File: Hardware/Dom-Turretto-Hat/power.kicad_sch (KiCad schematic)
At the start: 14 parts

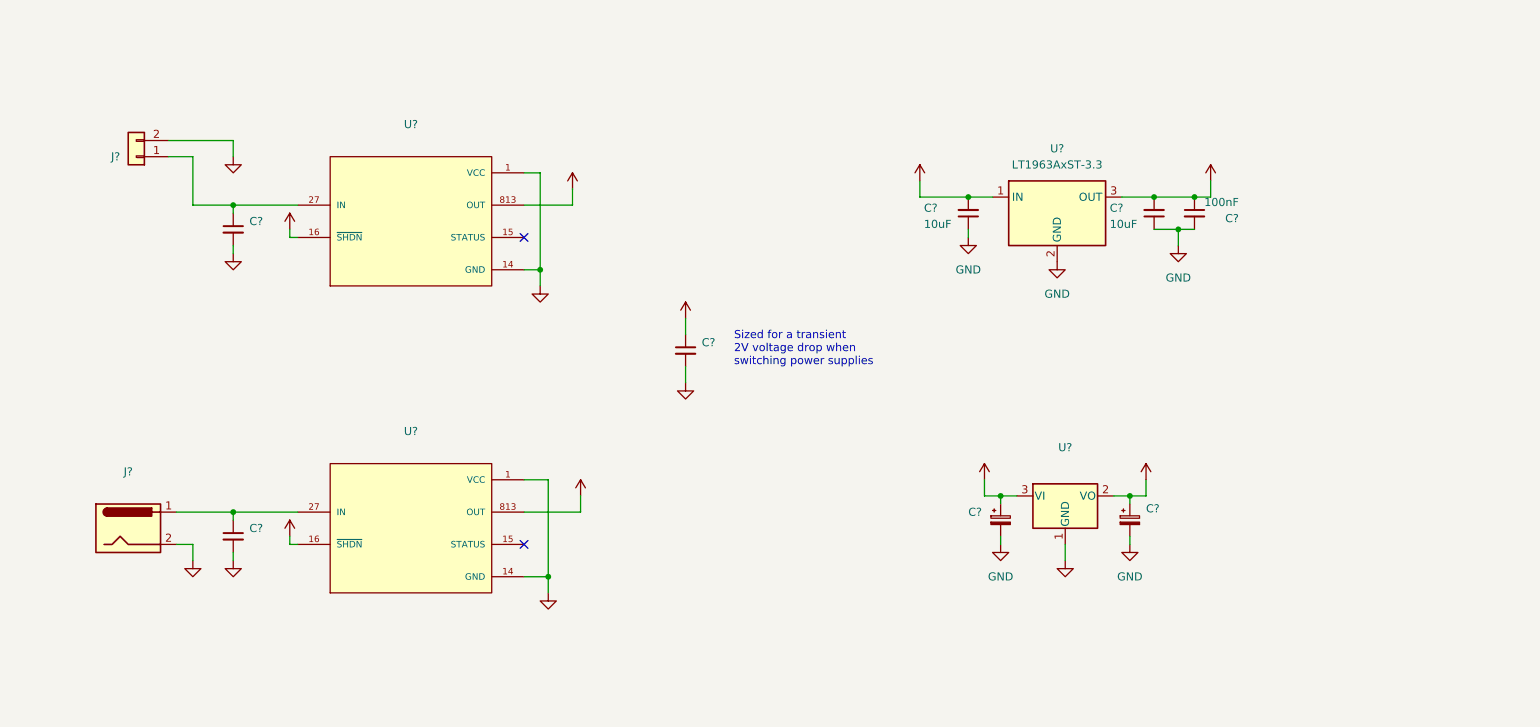
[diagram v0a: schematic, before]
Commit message: Add stepper motor drivers
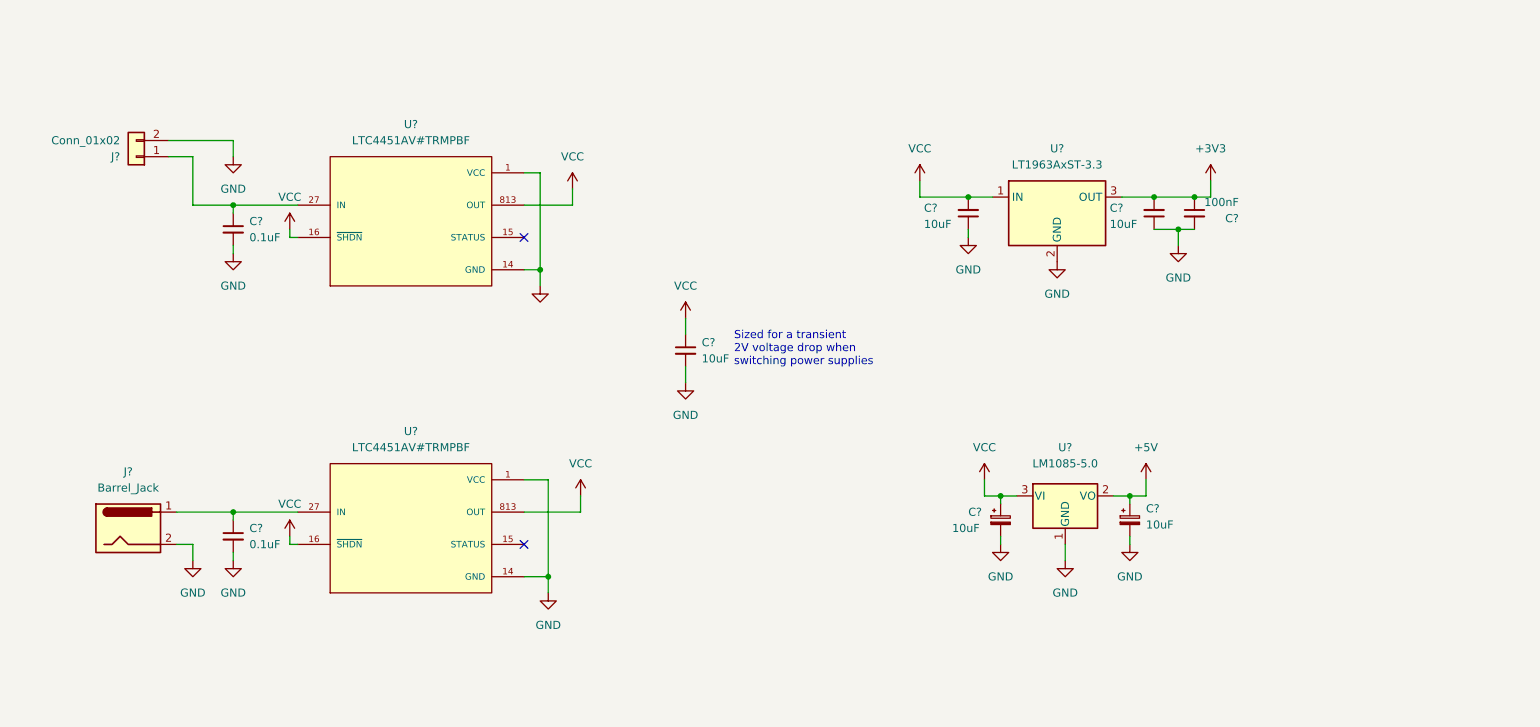
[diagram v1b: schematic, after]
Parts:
- C? (x3): value (none) -> 10uF
- C? (x2): value (none) -> 0.1uF
- J?: value (none) -> Conn_01x02
- J?: value (none) -> Barrel_Jack
- U?: value (none) -> LM1085-5.0
- U? (x2): value (none) -> LTC4451AV#TRMPBF; footprint (none) -> IC_LTC4451AV#TRMPBF
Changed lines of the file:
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@@
       (effects (font (size 1.27 1.27)) hide)
     )
-    (property "Value" "" (id 1) (at 179.07 60.96 0))
+    (property "Value" "VCC" (id 1) (at 179.07 60.96 0))
     (property "Footprint" "" (id 2) (at 179.07 66.04 0)
       (effects (font (size 1.27 1.27)) hide)
@@
       (effects (font (size 1.27 1.27)) (justify left))
     )
-    (property "Value" "" (id 1) (at 184.15 120.65 0)
+    (property "Value" "10uF" (id 1) (at 184.15 120.65 0)
       (effects (font (size 1.27 1.27)) (justify left))
     )
@@
       (effects (font (size 1.27 1.27)) hide)
     )
-    (property "Value" "" (id 1) (at 120.65 135.89 0))
+    (property "Value" "GND" (id 1) (at 120.65 135.89 0))
     (property "Footprint" "" (id 2) (at 120.65 130.81 0)
       (effects (font (size 1.27 1.27)) hide)
@@
       (effects (font (size 1.27 1.27)) hide)
     )
-    (property "Value" "" (id 1) (at 124.46 62.23 0))
+    (property "Value" "VCC" (id 1) (at 124.46 62.23 0))
     (property "Footprint" "" (id 2) (at 124.46 67.31 0)
       (effects (font (size 1.27 1.27)) hide)
@@
     (in_bom yes) (on_board yes) (fields_autoplaced)
     (property "Reference" "U?" (id 0) (at 201.93 107.95 0))
-    (property "Value" "" (id 1) (at 201.93 110.49 0))
+    (property "Value" "LM1085-5.0" (id 1) (at 201.93 110.49 0))
     (property "Footprint" "" (id 2) (at 201.93 109.22 0)
       (effects (font (size 1.27 1.27) italic) hide)
@@
       (effects (font (size 1.27 1.27)) hide)
     )
-    (property "Value" "" (id 1) (at 201.93 130.81 0))
+    (property "Value" "GND" (id 1) (at 201.93 130.81 0))
     (property "Footprint" "" (id 2) (at 201.93 125.73 0)
       (effects (font (size 1.27 1.27)) hide)
@@
       (effects (font (size 1.27 1.27)) hide)
     )
-    (property "Value" "" (id 1) (at 142.24 102.87 0))
+    (property "Value" "GND" (id 1) (at 142.24 102.87 0))
     (property "Footprint" "" (id 2) (at 142.24 97.79 0)
       (effects (font (size 1.27 1.27)) hide)
@@
       (effects (font (size 1.27 1.27)) (justify left))
     )
-    (property "Value" "" (id 1) (at 144.78 93.9862 0)
+    (property "Value" "10uF" (id 1) (at 144.78 93.9862 0)
       (effects (font (size 1.27 1.27)) (justify left))
     )
@@
       (effects (font (size 1.27 1.27)) hide)
     )
-    (property "Value" "" (id 1) (at 80.01 116.84 0))
+    (property "Value" "VCC" (id 1) (at 80.01 116.84 0))
     (property "Footprint" "" (id 2) (at 80.01 121.92 0)
       (effects (font (size 1.27 1.27)) hide)
@@
       (effects (font (size 1.27 1.27)) (justify left))
     )
-    (property "Value" "" (id 1) (at 214.63 120.1038 0)
+    (property "Value" "10uF" (id 1) (at 214.63 120.1038 0)
       (effects (font (size 1.27 1.27)) (justify left))
     )
@@
       (effects (font (size 1.27 1.27)) hide)
     )
-    (property "Value" "" (id 1) (at 64.77 130.81 0))
+    (property "Value" "GND" (id 1) (at 64.77 130.81 0))
     (property "Footprint" "" (id 2) (at 64.77 125.73 0)
       (effects (font (size 1.27 1.27)) hide)
@@
       (effects (font (size 1.27 1.27)) (justify left))
     )
-    (property "Value" "" (id 1) (at 73.66 123.1962 0)
+    (property "Value" "0.1uF" (id 1) (at 73.66 123.1962 0)
       (effects (font (size 1.27 1.27)) (justify left))
     )
@@
       (effects (font (size 1.27 1.27)) hide)
     )
-    (property "Value" "" (id 1) (at 71.12 130.81 0))
+    (property "Value" "GND" (id 1) (at 71.12 130.81 0))
     (property "Footprint" "" (id 2) (at 71.12 125.73 0)
       (effects (font (size 1.27 1.27)) hide)
@@
       (effects (font (size 1.27 1.27)) hide)
     )
-    (property "Value" "" (id 1) (at 189.23 107.95 0))
+    (property "Value" "VCC" (id 1) (at 189.23 107.95 0))
     (property "Footprint" "" (id 2) (at 189.23 113.03 0)
       (effects (font (size 1.27 1.27)) hide)
@@
       (effects (font (size 1.27 1.27)) hide)
     )
-    (property "Value" "" (id 1) (at 125.73 110.49 0))
+    (property "Value" "VCC" (id 1) (at 125.73 110.49 0))
     (property "Footprint" "" (id 2) (at 125.73 115.57 0)
       (effects (font (size 1.27 1.27)) hide)
@@
     (in_bom yes) (on_board yes) (fields_autoplaced)
     (property "Reference" "U?" (id 0) (at 99.06 57.15 0))
-    (property "Value" "" (id 1) (at 99.06 59.69 0))
-    (property "Footprint" "" (id 2) (at 99.06 72.39 0)
+    (property "Value" "LTC4451AV#TRMPBF" (id 1) (at 99.06 59.69 0))
+    (property "Footprint" "IC_LTC4451AV#TRMPBF" (id 2) (at 99.06 72.39 0)
       (effects (font (size 1.27 1.27)) (justify left bottom) hide)
     )
@@
       (effects (font (size 1.27 1.27)) hide)
     )
-    (property "Value" "" (id 1) (at 224.79 60.96 0))
+    (property "Value" "+3V3" (id 1) (at 224.79 60.96 0))
     (property "Footprint" "" (id 2) (at 224.79 66.04 0)
       (effects (font (size 1.27 1.27)) hide)
@@
       (effects (font (size 1.27 1.27)) hide)
     )
-    (property "Value" "" (id 1) (at 80.01 68.58 0))
+    (property "Value" "VCC" (id 1) (at 80.01 68.58 0))
     (property "Footprint" "" (id 2) (at 80.01 73.66 0)
       (effects (font (size 1.27 1.27)) hide)
@@
       (effects (font (size 1.27 1.27)) (justify left))
     )
-    (property "Value" "" (id 1) (at 53.34 59.6901 0)
+    (property "Value" "Conn_01x02" (id 1) (at 53.34 59.6901 0)
       (effects (font (size 1.27 1.27)) (justify left))
     )
@@
       (effects (font (size 1.27 1.27)) hide)
     )
-    (property "Value" "" (id 1) (at 214.63 107.95 0))
+    (property "Value" "+5V" (id 1) (at 214.63 107.95 0))
     (property "Footprint" "" (id 2) (at 214.63 113.03 0)
       (effects (font (size 1.27 1.27)) hide)
@@
       (effects (font (size 1.27 1.27)) hide)
     )
-    (property "Value" "" (id 1) (at 71.12 67.31 0))
+    (property "Value" "GND" (id 1) (at 71.12 67.31 0))
     (property "Footprint" "" (id 2) (at 71.12 62.23 0)
       (effects (font (size 1.27 1.27)) hide)
@@
     (in_bom yes) (on_board yes) (fields_autoplaced)
     (property "Reference" "U?" (id 0) (at 99.06 105.41 0))
-    (property "Value" "" (id 1) (at 99.06 107.95 0))
-    (property "Footprint" "" (id 2) (at 99.06 120.65 0)
+    (property "Value" "LTC4451AV#TRMPBF" (id 1) (at 99.06 107.95 0))
+    (property "Footprint" "IC_LTC4451AV#TRMPBF" (id 2) (at 99.06 120.65 0)
       (effects (font (size 1.27 1.27)) (justify left bottom) hide)
     )
@@
       (effects (font (size 1.27 1.27)) hide)
     )
-    (property "Value" "" (id 1) (at 71.12 82.55 0))
+    (property "Value" "GND" (id 1) (at 71.12 82.55 0))
     (property "Footprint" "" (id 2) (at 71.12 77.47 0)
       (effects (font (size 1.27 1.27)) hide)
@@
       (effects (font (size 1.27 1.27)) hide)
     )
-    (property "Value" "" (id 1) (at 142.24 82.55 0))
+    (property "Value" "VCC" (id 1) (at 142.24 82.55 0))
     (property "Footprint" "" (id 2) (at 142.24 87.63 0)
       (effects (font (size 1.27 1.27)) hide)
@@
     (in_bom yes) (on_board yes) (fields_autoplaced)
     (property "Reference" "J?" (id 0) (at 54.61 111.76 0))
-    (property "Value" "" (id 1) (at 54.61 114.3 0))
+    (property "Value" "Barrel_Jack" (id 1) (at 54.61 114.3 0))
     (property "Footprint" "" (id 2) (at 55.88 121.666 0)
       (effects (font (size 1.27 1.27)) hide)
@@
       (effects (font (size 1.27 1.27)) (justify left))
     )
-    (property "Value" "" (id 1) (at 73.66 74.9362 0)
-      (effects (font (size 1.27 1.27)) (justify left))
-    )
+    (property "Value" "0.1uF" (id 1) (at 73.66 74.9362 0)
+      (effects (font (size 1.27 1.27)) (justify left))
+    )

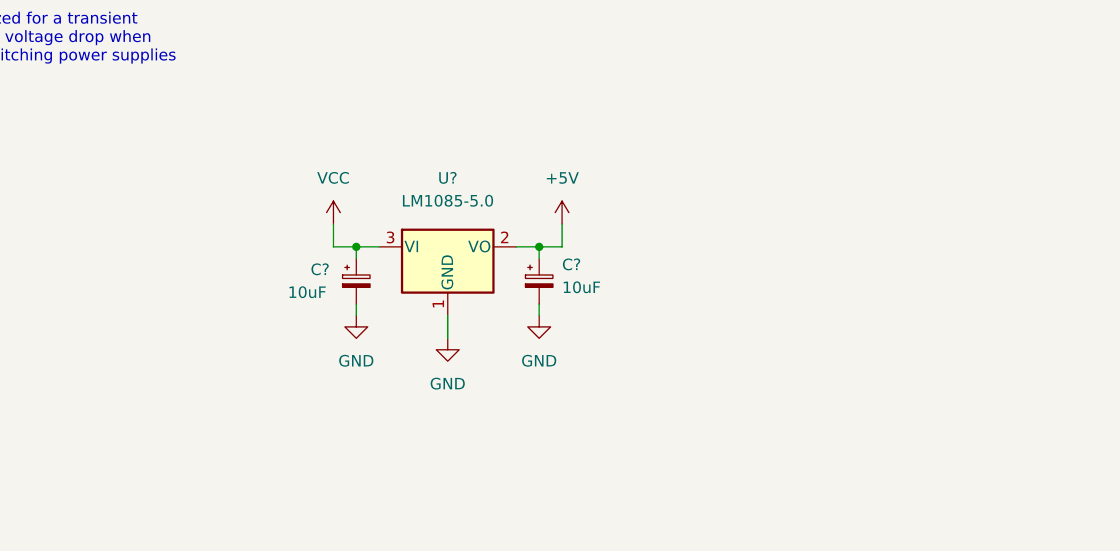
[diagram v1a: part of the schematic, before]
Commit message: Fix some stuff to make it HAT compatible
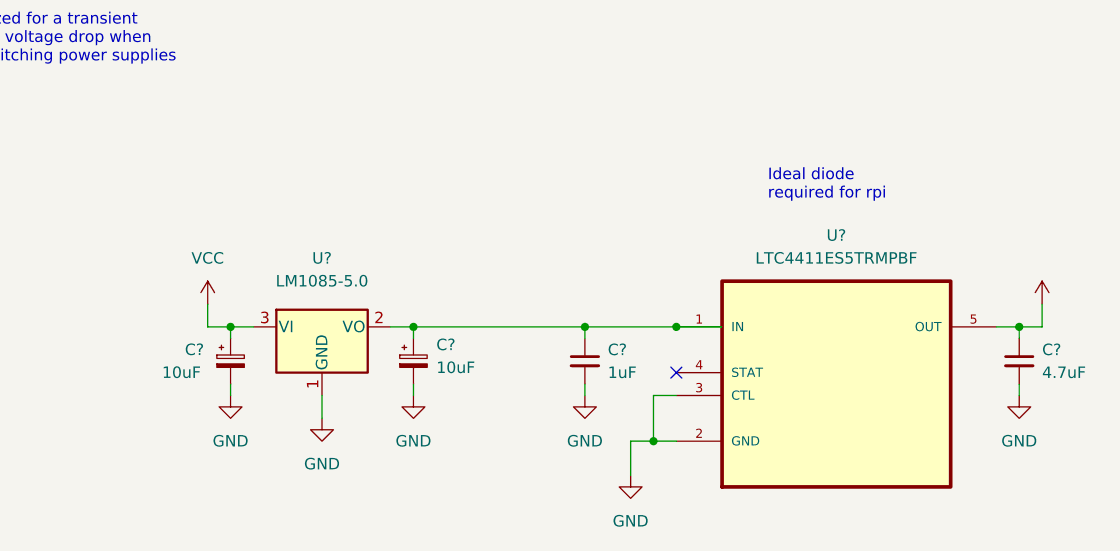
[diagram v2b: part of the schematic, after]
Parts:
- added C?: 1uF, Capacitor_SMD:C_0603_1608Metric, symbol Device:C_Small
- added C?: 4.7uF, Capacitor_SMD:C_0603_1608Metric, symbol Device:C_Small
- added U?: LTC4411ES5TRMPBF, Package_TO_SOT_SMD:SOT-23-5_HandSoldering, symbol LTC4411ES5TRMPBF:LTC4411ES5TRMPBF
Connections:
- net +5V: now also C?.1, U?.5 (OUT); no longer C?.1, U?.2 (VO)
- net GND: now also C?.2, C?.2, U?.2 (GND), U?.3 (CTL)
- new net: C?.1, C?.1, U?.1 (IN), U?.2 (VO)
- no-connect marks 2 -> 3
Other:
- note added: "Ideal diode required for rpi"
- moved on the sheet: C?, U?

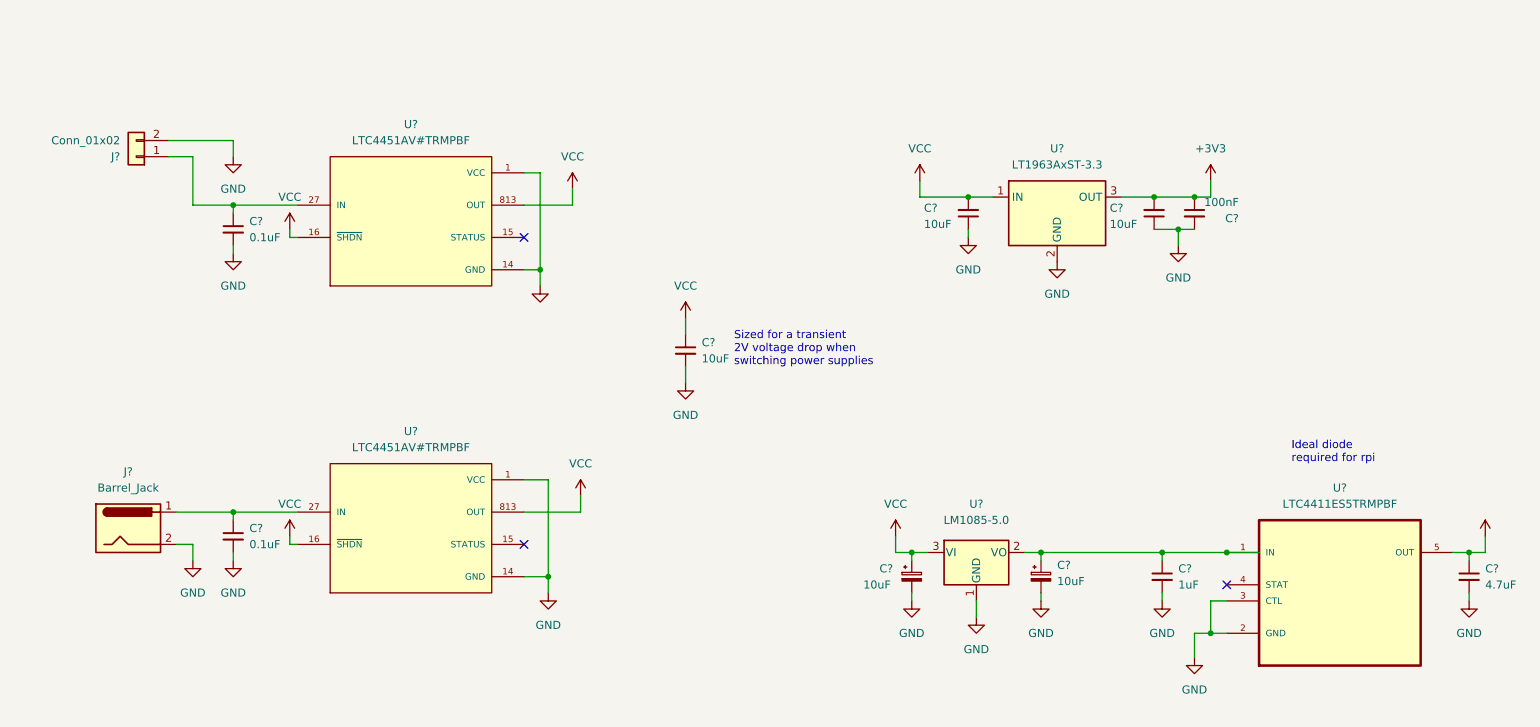
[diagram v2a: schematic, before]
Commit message: Add buck converter
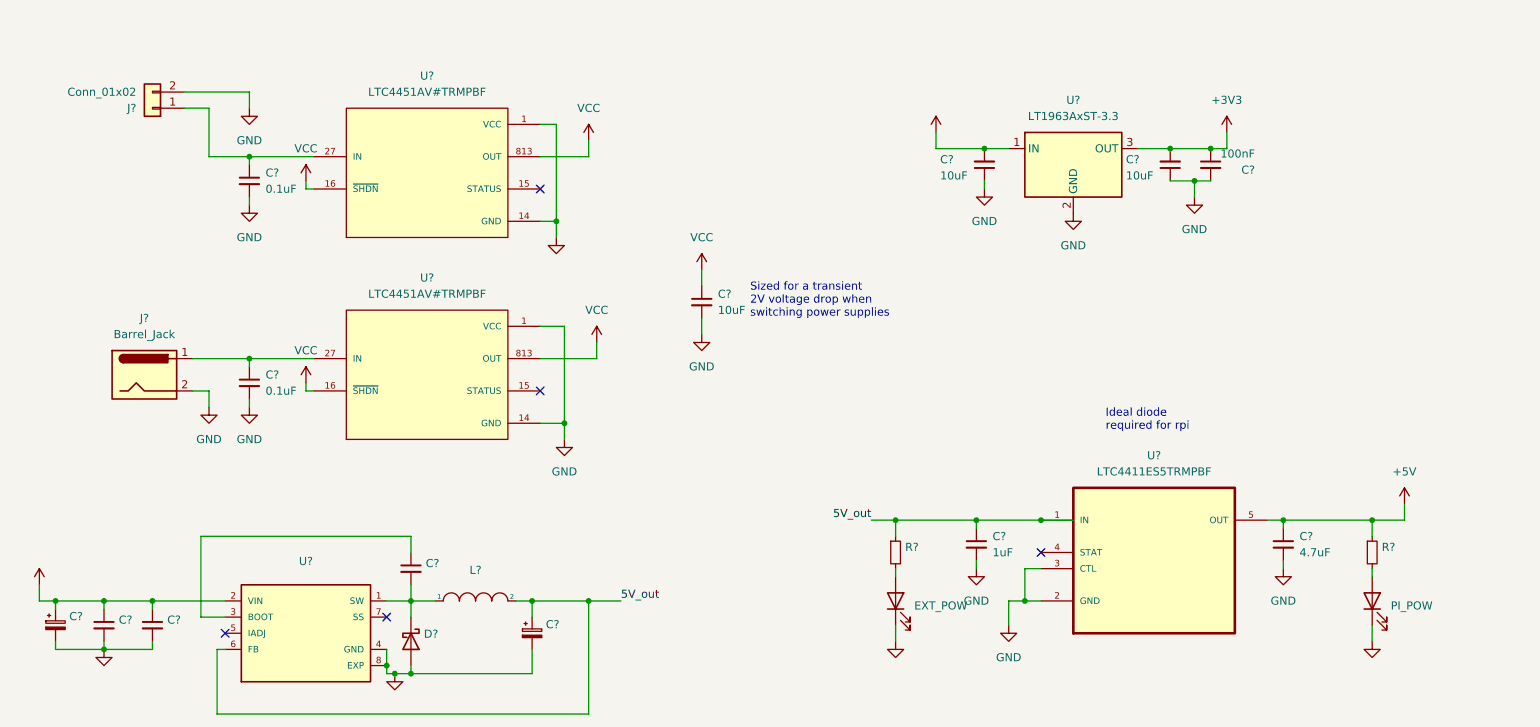
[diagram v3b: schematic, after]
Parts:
- removed C? (x2): 10uF, symbol Device:C_Polarized_Small
- removed U?: LM1085-5.0, symbol Regulator_Linear:LM1085-5.0
- added C? (x3): (no value), symbol Device:C_Small
- added C? (x2): (no value), symbol Device:C_Polarized_Small
- added D?: (no value), symbol Device:D_Schottky
- added EXT_POW, PI_POW: (no value), symbol Device:LED
- added L?: (no value), symbol pspice:INDUCTOR
- added R? (x2): (no value), symbol Device:R_Small
- added U?: (no value), symbol iclr:LM22679TJ-5.0{brace}slash}NOPB
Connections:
- net +5V: now also C?.2, U?.1 (IN), R?.1
- net GND: now also C?.2, C?.2, C?.2, C?.2, D?.2 (A), EXT_POW.1 (K), PI_POW.1 (K), U?.4 (GND), U?.8 (EXP)
- net VCC: now also C?.1, C?.1, C?.1, U?.2 (VIN); no longer C?.2, U?.1 (IN)
- net 5V_out: now reaches C?.1, U?.1 (IN)
- net 5V_out: now also C?.1, L?.2, R?.1, U?.6 (FB)
- new net: C?.2, D?.1 (K), L?.1, U?.1 (SW)
- new net: C?.1, U?.3 (BOOT)
- new net: EXT_POW.2 (A), R?.2
- new net: PI_POW.2 (A), R?.2
- no-connect marks 3 -> 5
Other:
- moved on the sheet: C?, J?, U?
